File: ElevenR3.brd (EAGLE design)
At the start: 68.6 x 53.3 mm, 63 parts, among them IC1 ATMEGA328P, IC2 ATMEGA16U2-MU, IC3 MC33269DT-5.0, IC4 LM358D, IC5 LP2985-33DBVR, J2 Analog, J3 Digital_8_13, J4 Digital_0_7, J5 DC_2_1MM, J6 Digital_0_7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

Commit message: Production release v2.0 after small revisions
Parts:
- J1: value Digital_0_7 -> Power
- LED1: value RX -> RX/GRN
- LED2: value TX -> TX/YEL
- renumbered J6 to J1, USB1 to P1
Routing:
- net DTR: track 7.68 -> 9.21 mm
- net GND: vias 17 -> 18
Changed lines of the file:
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@@
 <text x="21.082" y="43.561" size="0.8128" layer="21" font="vector" ratio="15" rot="R90">UBOOT</text>
 <text x="5.715" y="44.069" size="1.27" layer="21" font="vector" ratio="15">GND</text>
-<text x="12.192" y="42.545" size="0.762" layer="21" font="vector" ratio="15">ICSP-USB</text>
+<text x="12.446" y="42.418" size="0.762" layer="21" font="vector" ratio="15">ICSP-USB</text>
 <text x="22.86" y="28.956" size="1.3208" layer="21" font="vector" ratio="17">freetronics</text>
 <text x="63.754" y="16.637" size="1.7272" layer="22" font="vector" ratio="17" rot="SMR0">www.freetronics.com/eleven</text>
@@
 <attribute name="VALUE" x="21.844" y="24.003" size="0.4064" layer="27" font="vector"/>
 </element>
-<element name="LED1" library="freetronics" package="LED-0603" value="RX" x="66.548" y="18.034" smashed="yes" rot="R90">
+<element name="LED1" library="freetronics" package="LED-0603" value="RX/GRN" x="66.548" y="18.034" smashed="yes" rot="R90">
 <attribute name="NAME" x="64.008" y="18.2245" size="1.016" layer="25" rot="R180"/>
 <attribute name="VALUE" x="67.564" y="19.1135" size="0.4064" layer="27" rot="R180"/>
 </element>
-<element name="LED2" library="freetronics" package="LED-0603" value="TX" x="66.548" y="16.002" smashed="yes" rot="R90">
+<element name="LED2" library="freetronics" package="LED-0603" value="TX/YEL" x="66.548" y="16.002" smashed="yes" rot="R90">
 <attribute name="NAME" x="64.008" y="16.3195" size="1.016" layer="25" rot="R180"/>
 <attribute name="VALUE" x="67.564" y="17.0815" size="0.4064" layer="27" rot="R180"/>
@@
 <attribute name="VALUE" x="11.049" y="44.704" size="0.4064" layer="27" font="vector" rot="R90"/>
 </element>
-<element name="J6" library="freetronics" package="1X08" value="Digital_0_7" x="27.94" y="2.54" smashed="yes">
+<element name="J1" library="freetronics" package="1X08" value="Power" x="27.94" y="2.54" smashed="yes">
 <attribute name="NAME" x="30.6578" y="3.3528" size="1.016" layer="25" ratio="10"/>
 <attribute name="VALUE" x="26.67" y="-0.635" size="1.27" layer="27"/>
 </element>
-<element name="USB1" library="freetronics-jon" package="USB-MICROB-MB05PMXX" value="USB-6PSMT" x="1.524" y="38.1" smashed="yes" rot="R270">
+<element name="P1" library="freetronics-jon" package="USB-MICROB-MB05PMXX" value="USB-6PSMT" x="1.524" y="38.1" smashed="yes" rot="R270">
 <attribute name="NAME" x="1.956" y="37.75" size="1.016" layer="25" ratio="12"/>
 <attribute name="VALUE" x="-0.651" y="40.005" size="0.762" layer="27" rot="R270"/>
@@
 <via x="24.511" y="46.99" extent="1-16" drill="0.5"/>
 <via x="22.352" y="31.877" extent="1-16" drill="0.5"/>
-<contactref element="J6" pad="5"/>
+<contactref element="J1" pad="5"/>
 <via x="22.098" y="10.668" extent="1-16" drill="0.5"/>
 <via x="21.336" y="11.43" extent="1-16" drill="0.5"/>
@@
 <wire x1="24.638" y1="12.534" x2="24.892" y2="12.28" width="0.4064" layer="1"/>
 <wire x1="24.892" y1="12.28" x2="24.892" y2="11.29" width="0.4064" layer="1"/>
-<contactref element="J6" pad="2"/>
+<contactref element="J1" pad="2"/>
 <wire x1="30.48" y1="2.54" x2="28.321" y2="4.699" width="0.4064" layer="1"/>
 <wire x1="28.321" y1="4.699" x2="28.321" y2="8.128" width="0.4064" layer="1"/>
@@
 <via x="47.244" y="23.622" extent="1-16" drill="0.5"/>
 <via x="22.098" y="41.1988" extent="1-16" drill="0.5"/>
-<contactref element="J6" pad="3"/>
+<contactref element="J1" pad="3"/>
 </signal>
 <signal name="GND">
@@
 <vertex x="0" y="2.54"/>
 </polygon>
-<contactref element="J6" pad="7"/>
-<contactref element="J6" pad="6"/>
+<contactref element="J1" pad="7"/>
+<contactref element="J1" pad="6"/>
 <via x="17.653" y="49.403" extent="1-16" drill="0.5"/>
 <via x="1.651" y="49.403" extent="1-16" drill="0.5"/>
 <via x="12.065" y="49.403" extent="1-16" drill="0.5"/>
+<via x="6.35" y="33.274" extent="1-16" drill="0.5"/>
 </signal>
 <signal name="3V3">
@@
 <via x="7.62" y="27.178" extent="1-16" drill="0.5"/>
 <via x="21.463" y="19.558" extent="1-16" drill="0.5"/>
-<contactref element="J6" pad="4"/>
+<contactref element="J1" pad="4"/>
 </signal>
 <signal name="VIN">
@@
 <via x="20.701" y="8.255" extent="1-16" drill="0.5"/>
 <via x="21.463" y="7.62" extent="1-16" drill="0.5"/>
-<contactref element="J6" pad="8"/>
+<contactref element="J1" pad="8"/>
 <wire x1="23.79" y1="2.54" x2="22.352" y2="3.978" width="1.4224" layer="1"/>
 <wire x1="22.352" y1="3.978" x2="22.352" y2="6.604" width="1.4224" layer="1"/>
@@
 <wire x1="23.368" y1="44.577" x2="23.368" y2="45.085" width="0.254" layer="1"/>
 <wire x1="23.368" y1="45.085" x2="23.622" y2="45.339" width="0.254" layer="1"/>
+<wire x1="22.098" y1="42.799" x2="23.622" y2="42.799" width="0.4064" layer="1"/>
 </signal>
 <signal name="USBRXD">
@@
 <wire x1="9.144" y1="35.56" x2="9.398" y2="35.726" width="0.4064" layer="1"/>
 <wire x1="2.286" y1="46.156" x2="2.286" y2="47.117" width="0.4064" layer="1"/>
-<contactref element="USB1" pad="TAB2"/>
-<contactref element="USB1" pad="TAB1"/>
+<contactref element="P1" pad="TAB2"/>
+<contactref element="P1" pad="TAB1"/>
 <wire x1="2.286" y1="46.156" x2="1.524" y2="45.394" width="0.4064" layer="1"/>
 <wire x1="1.524" y1="45.394" x2="1.524" y2="41.925" width="0.4064" layer="1"/>
@@
 <wire x1="4.318" y1="41.656" x2="1.793" y2="41.656" width="0.8128" layer="1"/>
 <wire x1="1.524" y1="39.37" x2="1.524" y2="36.83" width="0.8128" layer="1"/>
-<contactref element="USB1" pad="FIX1"/>
-<contactref element="USB1" pad="FIX2"/>
-<contactref element="USB1" pad="PIN1"/>
-<contactref element="USB1" pad="PIN2"/>
+<contactref element="P1" pad="FIX1"/>
+<contactref element="P1" pad="FIX2"/>
+<contactref element="P1" pad="PIN1"/>
+<contactref element="P1" pad="PIN2"/>
 <wire x1="1.524" y1="39.37" x2="1.524" y2="39.4" width="0.8128" layer="1"/>
 <wire x1="1.524" y1="39.4" x2="1.524" y2="41.525" width="0.8128" layer="1"/>
@@
 <wire x1="9.31" y1="37.426" x2="9.398" y2="37.426" width="0.4064" layer="1"/>
 <wire x1="9.398" y1="37.426" x2="11.176" y2="37.426" width="0.4064" layer="1"/>
-<contactref element="USB1" pad="D+"/>
+<contactref element="P1" pad="D+"/>
 <wire x1="4.099" y1="38.1" x2="8.636" y2="38.1" width="0.3048" layer="1"/>
 </signal>
@@
 <wire x1="8.524" y1="38.75" x2="9.31" y2="39.536" width="0.3048" layer="1"/>
 <wire x1="9.398" y1="39.536" x2="9.31" y2="39.536" width="0.4064" layer="1"/>
-<contactref element="USB1" pad="D-"/>
+<contactref element="P1" pad="D-"/>
 <wire x1="9.398" y1="39.536" x2="11.176" y2="39.536" width="0.4064" layer="1"/>
 <wire x1="4.099" y1="38.75" x2="8.524" y2="38.75" width="0.3048" layer="1"/>
@@
 <via x="1.651" y="29.337" extent="1-16" drill="0.5"/>
 <via x="1.651" y="30.607" extent="1-16" drill="0.5"/>
-<contactref element="USB1" pad="VBUS"/>
+<contactref element="P1" pad="VBUS"/>
 <wire x1="4.099" y1="39.4" x2="5.618" y2="39.4" width="0.4064" layer="1"/>
 <wire x1="5.618" y1="39.4" x2="6.056" y2="39.838" width="0.4064" layer="1"/>
@@
 <contactref element="IC2" pad="28"/>
 <contactref element="SJ2" pad="1"/>
-<contactref element="USB1" pad="GND"/>
+<contactref element="P1" pad="GND"/>
 <wire x1="6.858" y1="36.576" x2="7.874" y2="36.576" width="0.6096" layer="1"/>
 <wire x1="14.101" y1="39.874" x2="14.718" y2="39.874" width="0.254" layer="1"/>
@@
 </signal>
 </signals>
+<errors>
+</errors>
 </board>
 </drawing>

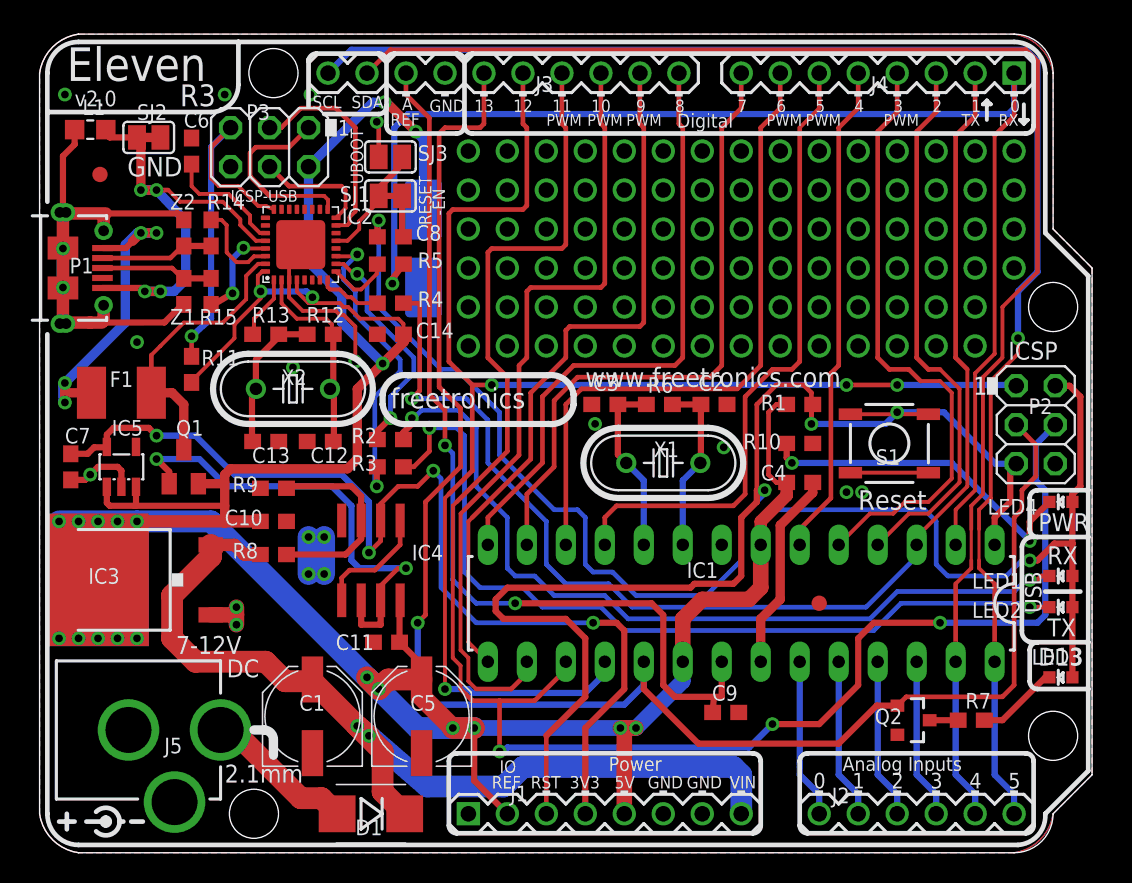
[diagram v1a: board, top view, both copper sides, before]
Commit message: Replaced most parts using SuperHouse library to add 3D models
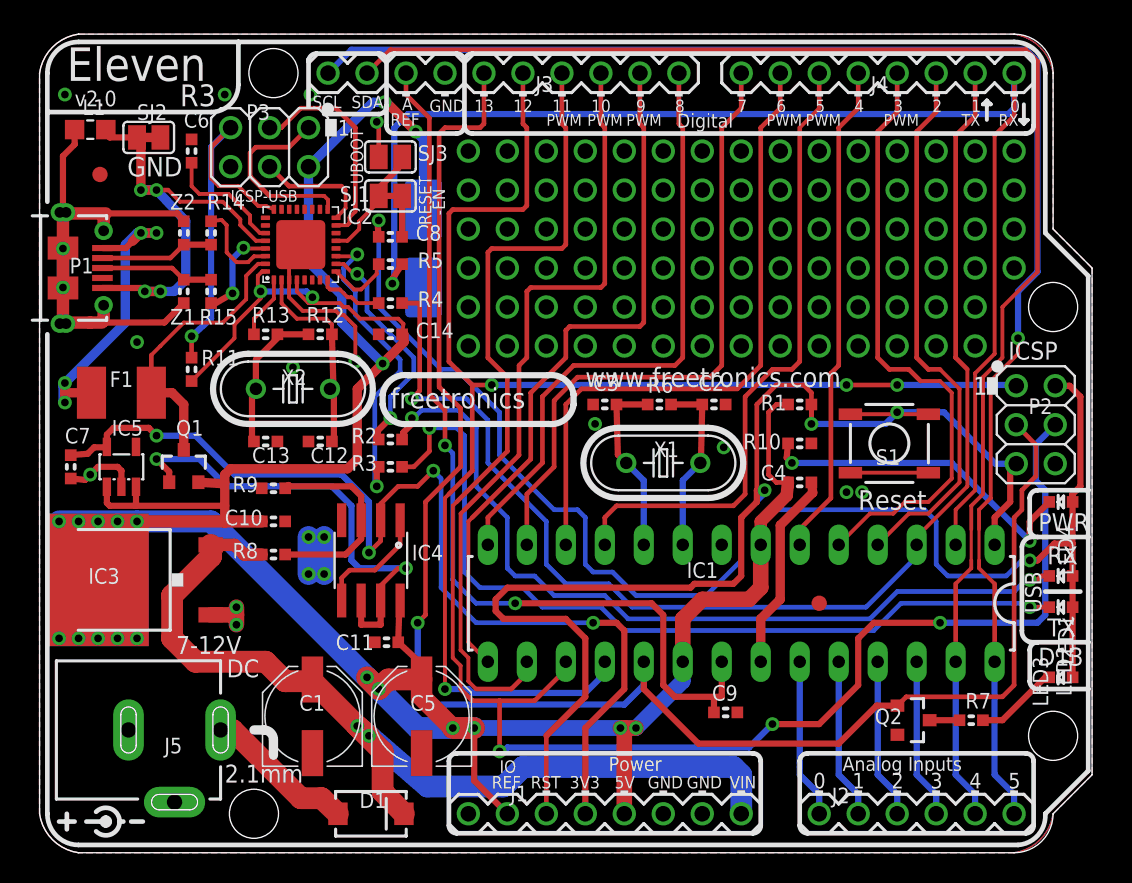
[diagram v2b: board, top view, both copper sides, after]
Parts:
- C10, C11, C12, C13, C14, C2, C3, C4, C6, C7, C8, C9: device freetronics:0603 -> SuperHouse-DiscreteSemi:C0603
- D1: device freetronics:SMB-DIODE -> SuperHouse-DiscreteSemi:SMA-DIODE
- IC1: device freetronics:DIL28-3 -> SuperHouse-MCUs:DIL28-3
- IC2: device freetronics-jon:ATMEL_QFN32 -> SuperHouse-MCUs:ATMEL_QFN32
- IC3: device linear:DPACK -> SuperHouse-Regulators:DPACK
- IC4: device linear:SO08 -> SuperHouse-ICs:SO08
- IC5: device freetronics-jon:TEXAS_SOT23-DBV -> SuperHouse-Regulators:TEXAS_SOT23-DBV
- J1, J4: device freetronics:1X08 -> SuperHouse-Connectors:1X08-S
- J2: device freetronics:1X06 -> SuperHouse-Connectors:1X06-S
- J3: device freetronics-original:1X10 -> SuperHouse-Connectors:1X10-S
- J5: device freetronics:POWER_JACK_PTH -> SuperHouse-Connectors:POWER_JACK_SLOTS
- L1: device freetronics-master-v1:0805-LARGE -> SuperHouse-DiscreteSemi:0805-LARGE
- LED1, LED2, LED3, LED4: device freetronics:LED-0603 -> SuperHouse-LEDs:LED-0603
- P1: value USB-6PSMT -> USB-6P-SMT; device freetronics-jon:USB-MICROB-MB05PMXX -> SuperHouse-Connectors:USB-MICROB-MB05PMXX
- P2, P3: device pinhead:2X03 -> SuperHouse-Connectors:2X03PTH
- Q1: device freetronics-master-v1:SOT23 -> SuperHouse-DiscreteSemi:SOT23-3
- Q2: device freetronics:SOT23-3 -> SuperHouse-DiscreteSemi:SOT23-3
- R1, R10, R11, R12, R13, R14, R15, R2, R3, R4, R5, R6, R7, R8, R9: device freetronics:0603 -> SuperHouse-DiscreteSemi:R0603
- S1: device freetronics:TACTILE_SWITCH_SMD -> SuperHouse-Switches:TACTILE_SMD-6MM
- X1, X2: device freetronics-master-v1:HC49U-V -> SuperHouse-Oscillators:HC49U-V
- Z1, Z2: device freetronics:0603 -> SuperHouse-DiscreteSemi:TVS0603
- turned D1 to 0 degrees
- turned LED1 to 180 degrees
- turned LED2 to 180 degrees
- turned LED3 to 180 degrees
- turned LED4 to 180 degrees
